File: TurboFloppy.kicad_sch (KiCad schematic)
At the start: 20 parts, among them CN1 SOCKET_28PIN, CN2 PIN_HEADER_28PIN, J1 C16-Exp-Port, Q1 NPN, U1 8255, U2 74LS30, U4 74LS27, U5 74LS10

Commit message: Replace cartridge connector
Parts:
- removed Q1: NPN, Package_TO_SOT_THT:TO-92_HandSolder, symbol Simulation_SPICE:NPN
- added Q1: BC547, Package_TO_SOT_THT:TO-92_HandSolder, symbol Transistor_BJT:BC547
- CN1: renamed from J1; value C16-Exp-Port -> EXPANSION_PORT
- renumbered CN1 to CN2, CN2 to CN3
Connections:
- net GND: now also Q1.3 (E)
- net at R2.2: now also Q1.2 (B)
- net at R1.1, U1.35 (RESET): now also Q1.1 (C)
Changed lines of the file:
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@@
 	(title_block
 		(title "Intel 8255 Interface for the Commodore 16, 116 and Plus/4")
-		(date "2024-07-13")
+		(date "2024-07-14")
 		(rev "1git")
 		(company "SukkoPera")
 		(comment 1 "Based on the article published in Rádiótechnika 1988/12 by Ferenc Garay and Dr. János Rohonczy.")
 		(comment 2 "http://plus4world.powweb.com/publications/Radiotechnika_1988_december")
+		(comment 3 "Licensed under CC BY-NC-SA 4.0")
 	)
 	(junction
@@
 	)
 	(symbol
+		(lib_id "Transistor_BJT:BC547")
+		(at 115.57 36.83 0)
+		(unit 1)
+		(exclude_from_sim no)
+		(in_bom yes)
+		(on_board yes)
+		(dnp no)
+		(fields_autoplaced yes)
+		(property "Reference" "Q1"
+			(at 120.65 35.5599 0)
+			(effects
+				(font
+					(size 1.27 1.27)
+				)
+				(justify left)
+			)
+		)
+		(property "Value" "BC547"
+			(at 120.65 38.0999 0)
+			(effects
+				(font
+					(size 1.27 1.27)
+				)
+				(justify left)
+			)
+		)
+		(property "Footprint" "Package_TO_SOT_THT:TO-92_HandSolder"
+			(at 120.65 38.735 0)
+			(effects
+				(font
+					(size 1.27 1.27)
+					(italic yes)
+				)
+				(justify left)
+				(hide yes)
+			)
+		)
+		(property "Datasheet" "https://www.onsemi.com/pub/Collateral/BC550-D.pdf"
+			(at 115.57 36.83 0)
+			(effects
+				(font
+					(size 1.27 1.27)
+				)
+				(justify left)
+				(hide yes)
+			)
+		)
+		(property "Description" "0.1A Ic, 45V Vce, Small Signal NPN Transistor, TO-92"
+			(at 115.57 36.83 0)
+			(effects
+				(font
+					(size 1.27 1.27)
+				)
+				(hide yes)
+			)
+		)
+		(pin "1"
+		)
+		(pin "2"
+		)
+		(pin "3"
+		)
+		(instances
+			(project ""
+				(path "/0a31112a-e046-4d46-8b9e-0685d05e37f7"
+					(reference "Q1")
+					(unit 1)
+				)
+			)
+		)
+	)
+	(symbol
 		(lib_id "74xx:74LS10")
 		(at 256.54 142.24 0)
@@
 		(on_board yes)
 		(dnp no)
-		(property "Reference" "CN2"
+		(property "Reference" "CN3"
 			(at 259.08 41.91 0)
 			(effects
@@
 			(project ""
 				(path "/0a31112a-e046-4d46-8b9e-0685d05e37f7"
-					(reference "CN2")
+					(reference "CN3")
 					(unit 1)
 				)
@@
 		(dnp no)
 		(fields_autoplaced yes)
-		(property "Reference" "J1"
+		(property "Reference" "CN1"
 			(at 54.61 24.13 0)
 			(effects
@@
 			)
 		)
-		(property "Value" "C16-Exp-Port"
+		(property "Value" "EXPANSION_PORT"
 			(at 54.61 26.67 0)
 			(effects
@@
 			(project ""
 				(path "/0a31112a-e046-4d46-8b9e-0685d05e37f7"
-					(reference "J1")
+					(reference "CN1")
 					(unit 1)
 				)
@@
 	)
 	(symbol
-		(lib_id "Simulation_SPICE:NPN")
-		(at 115.57 36.83 0)
-		(unit 1)
-		(exclude_from_sim no)
-		(in_bom yes)
-		(on_board yes)
-		(dnp no)
-		(property "Reference" "Q1"
-			(at 111.506 39.624 0)
-			(effects
-				(font
-					(size 1.27 1.27)
-				)
-				(justify left)
-			)
-		)
-		(property "Value" "NPN"
-			(at 109.982 41.91 0)
-			(effects
-				(font
-					(size 1.27 1.27)
-				)
-				(justify left)
-			)
-		)
-		(property "Footprint" "Package_TO_SOT_THT:TO-92_HandSolder"
-			(at 179.07 36.83 0)
-			(effects
-				(font
-					(size 1.27 1.27)
-				)
-				(hide yes)
-			)
-		)
-		(property "Datasheet" "https://ngspice.sourceforge.io/docs/ngspice-html-manual/manual.xhtml#cha_BJTs"
-			(at 179.07 36.83 0)
-			(effects
-				(font
-					(size 1.27 1.27)
-				)
-				(hide yes)
-			)
-		)
-		(property "Description" "Bipolar transistor symbol for simulation only, substrate tied to the emitter"
-			(at 115.57 36.83 0)
-			(effects
-				(font
-					(size 1.27 1.27)
-				)
-				(hide yes)
-			)
-		)
-		(property "Sim.Device" "NPN"
-			(at 115.57 36.83 0)
-			(effects
-				(font
-					(size 1.27 1.27)
-				)
-				(hide yes)
-			)
-		)
-		(property "Sim.Type" "GUMMELPOON"
-			(at 115.57 36.83 0)
-			(effects
-				(font
-					(size 1.27 1.27)
-				)
-				(hide yes)
-			)
-		)
-		(property "Sim.Pins" "1=C 2=B 3=E"
-			(at 115.57 36.83 0)
-			(effects
-				(font
-					(size 1.27 1.27)
-				)
-				(hide yes)
-			)
-		)
-		(pin "3"
-		)
-		(pin "2"
-		)
-		(pin "1"
-		)
-		(instances
-			(project ""
-				(path "/0a31112a-e046-4d46-8b9e-0685d05e37f7"
-					(reference "Q1")
-					(unit 1)
-				)
-			)
-		)
-	)
-	(symbol
 		(lib_id "power:+5V")
 		(at 267.97 39.37 0)
@@
 		(dnp no)
 		(fields_autoplaced yes)
-		(property "Reference" "CN1"
+		(property "Reference" "CN2"
 			(at 217.17 60.9599 0)
 			(effects
@@
 			(project ""
 				(path "/0a31112a-e046-4d46-8b9e-0685d05e37f7"
-					(reference "CN1")
+					(reference "CN2")
 					(unit 1)
 				)

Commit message: Who knows?
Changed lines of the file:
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@@
 		(rev "1git")
 		(company "SukkoPera")
-		(comment 1 "Based on the article published in Rádiótechnika 1988/12 by Ferenc Garay and Dr. János Rohonczy.")
+		(comment 1 "Based on the article published in Rádiótechnika 1988/12 by Ferenc Garay and Dr. János Rohonczy")
 		(comment 2 "http://plus4world.powweb.com/publications/Radiotechnika_1988_december")
 		(comment 3 "Licensed under CC BY-NC-SA 4.0")
@@
 		(on_board yes)
 		(dnp no)
-		(fields_autoplaced yes)
 		(property "Reference" "Q1"
-			(at 120.65 35.5599 0)
+			(at 111.506 39.624 0)
 			(effects
 				(font
@@
 		)
 		(property "Value" "BC547"
-			(at 120.65 38.0999 0)
+			(at 107.696 41.91 0)
 			(effects
 				(font

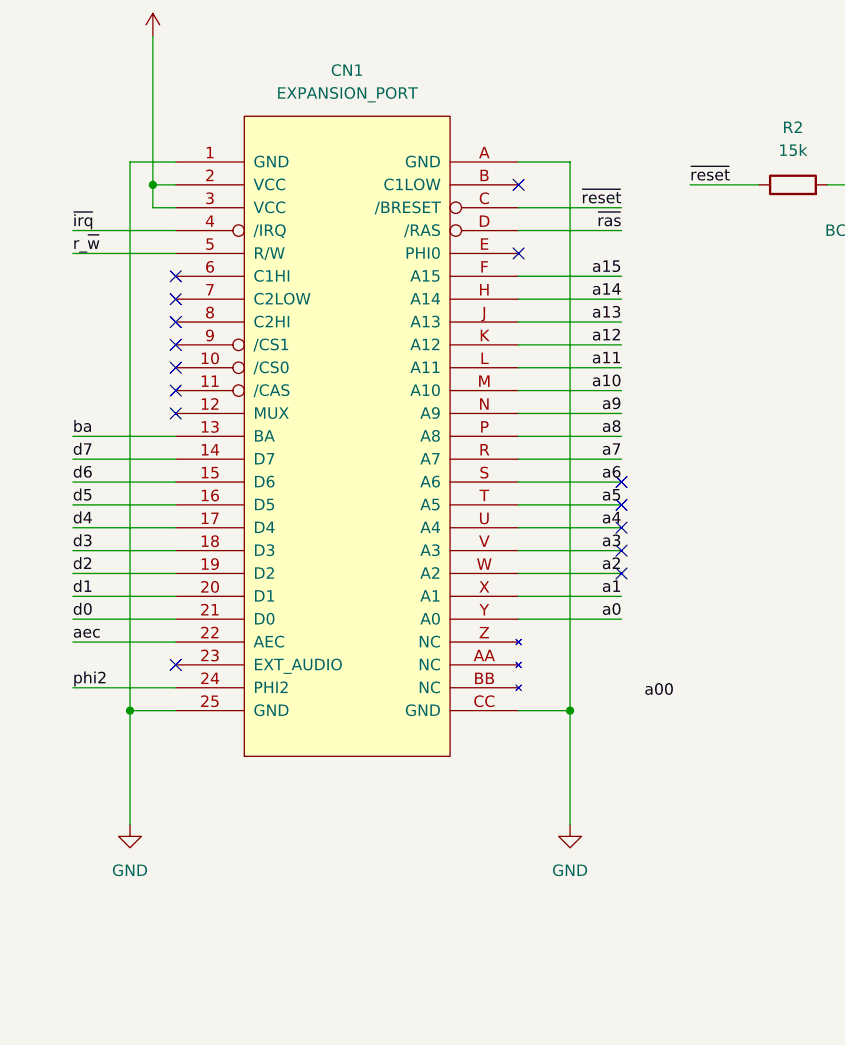
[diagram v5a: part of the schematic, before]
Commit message: Fix connector symbol and ERC
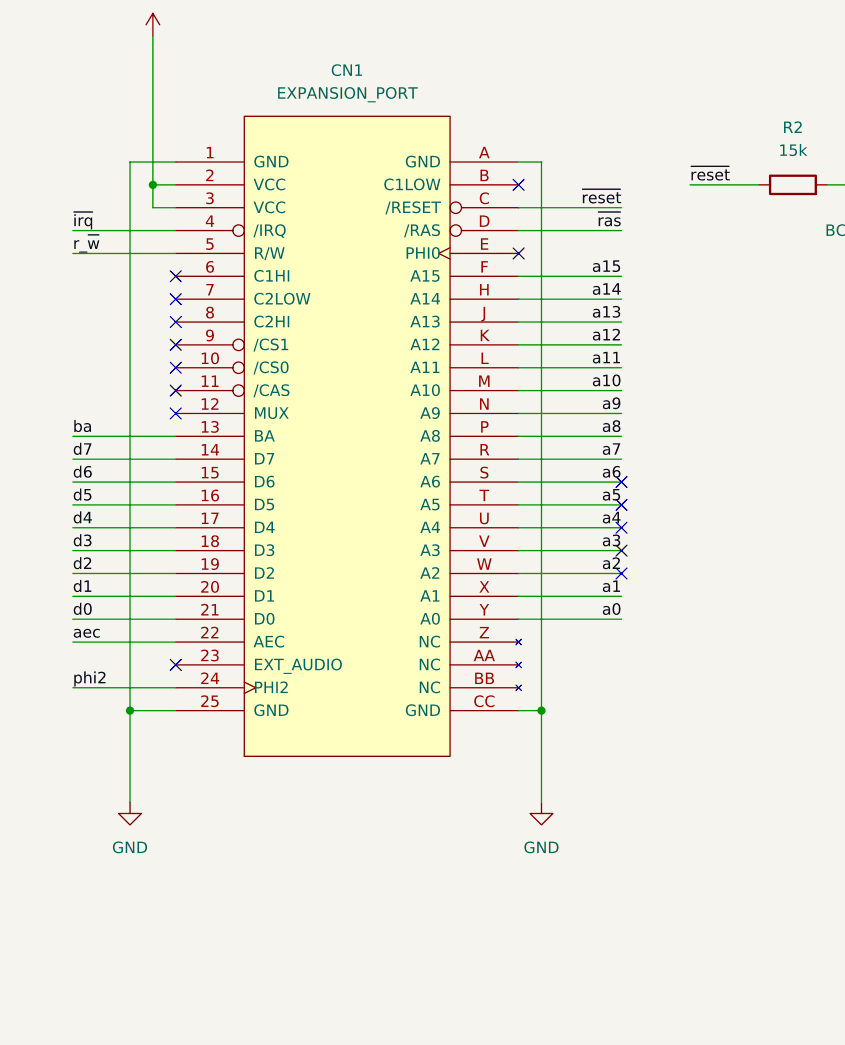
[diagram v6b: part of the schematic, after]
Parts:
- CN1: footprint TurboFloppy:C16_Cart_Conn -> MODULE
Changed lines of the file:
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@@
 	)
 	(junction
-		(at 79.375 95.25)
-		(diameter 0)
-		(color 0 0 0 0)
-	)
-	(junction
 		(at 35.56 160.02)
 		(diameter 0)
@@
 	)
 	(junction
+		(at 76.2 95.25)
+		(diameter 0)
+		(color 0 0 0 0)
+	)
+	(junction
 		(at 250.19 81.28)
 		(diameter 0)
@@
 	(wire
 		(pts
+			(xy 76.2 34.29) (xy 76.2 95.25)
+		)
+		(stroke
+			(width 0)
+			(type default)
+		)
+	)
+	(wire
+		(pts
 			(xy 24.13 72.39) (xy 35.56 72.39)
 		)
@@
 	(wire
 		(pts
+			(xy 73.66 95.25) (xy 76.2 95.25)
+		)
+		(stroke
+			(width 0)
+			(type default)
+		)
+	)
+	(wire
+		(pts
 			(xy 229.87 144.78) (xy 248.92 144.78)
 		)
@@
 	(wire
 		(pts
-			(xy 79.375 95.25) (xy 73.66 95.25)
-		)
-		(stroke
-			(width 0)
-			(type default)
-		)
-	)
-	(wire
-		(pts
 			(xy 170.18 35.56) (xy 180.34 35.56)
 		)
@@
 	(wire
 		(pts
-			(xy 79.375 34.29) (xy 79.375 95.25)
-		)
-		(stroke
-			(width 0)
-			(type default)
-		)
-	)
-	(wire
-		(pts
 			(xy 85.09 80.01) (xy 73.66 80.01)
 		)
@@
 	(wire
 		(pts
+			(xy 76.2 95.25) (xy 76.2 105.41)
+		)
+		(stroke
+			(width 0)
+			(type default)
+		)
+	)
+	(wire
+		(pts
 			(xy 201.93 81.28) (xy 210.82 81.28)
 		)
@@
 	(wire
 		(pts
-			(xy 30.48 95.25) (xy 30.48 107.95)
+			(xy 30.48 95.25) (xy 30.48 105.41)
 		)
 		(stroke
@@
 	(wire
 		(pts
-			(xy 73.66 34.29) (xy 79.375 34.29)
+			(xy 73.66 34.29) (xy 76.2 34.29)
 		)
 		(stroke
@@
 	(wire
 		(pts
-			(xy 79.375 95.25) (xy 79.375 107.95)
-		)
-		(stroke
-			(width 0)
-			(type default)
-		)
-	)
-	(wire
-		(pts
 			(xy 106.68 186.69) (xy 106.68 187.96)
 		)
@@
 		)
 	)
-	(label "a00"
-		(at 87.63 93.98 0)
-		(fields_autoplaced yes)
-		(effects
-			(font
-				(size 1.27 1.27)
-			)
-			(justify left bottom)
-		)
-	)
 	(label "pb2"
 		(at 274.32 76.2 180)
@@
 	(symbol
 		(lib_id "power:GND")
-		(at 30.48 107.95 0)
+		(at 30.48 105.41 0)
+		(mirror y)
 		(unit 1)
 		(exclude_from_sim no)
@@
 		(on_board yes)
 		(dnp no)
-		(fields_autoplaced yes)
 		(property "Reference" "#PWR04"
-			(at 30.48 114.3 0)
+			(at 30.48 111.76 0)
 			(effects
 				(font
@@
 		)
 		(property "Value" "GND"
-			(at 30.48 113.03 0)
+			(at 30.48 110.49 0)
 			(effects
 				(font
@@
 		)
 		(property "Footprint" ""
-			(at 30.48 107.95 0)
+			(at 30.48 105.41 0)
 			(effects
 				(font
@@
 		)
 		(property "Datasheet" ""
-			(at 30.48 107.95 0)
+			(at 30.48 105.41 0)
 			(effects
 				(font
@@
 		)
 		(property "Description" "Power symbol creates a global label with name \"GND\" , ground"
-			(at 30.48 107.95 0)
+			(at 30.48 105.41 0)
 			(effects
 				(font
@@
 			)
 		)
-		(property "Footprint" "TurboFloppy:C16_Cart_Conn"
+		(property "Footprint" "MODULE"
 			(at 54.61 106.68 0)
 			(effects
@@
 	(symbol
 		(lib_id "power:GND")
-		(at 79.375 107.95 0)
+		(at 76.2 105.41 0)
 		(mirror y)
 		(unit 1)
@@
 		(fields_autoplaced yes)
 		(property "Reference" "#PWR05"
-			(at 79.375 114.3 0)
+			(at 76.2 111.76 0)
 			(effects
 				(font
@@
 		)
 		(property "Value" "GND"
-			(at 79.375 113.03 0)
+			(at 76.2 110.49 0)
 			(effects
 				(font
@@
 		)
 		(property "Footprint" ""
-			(at 79.375 107.95 0)
+			(at 76.2 105.41 0)
 			(effects
 				(font
@@
 		)
 		(property "Datasheet" ""
-			(at 79.375 107.95 0)
+			(at 76.2 105.41 0)
 			(effects
 				(font
@@
 		)
 		(property "Description" "Power symbol creates a global label with name \"GND\" , ground"
-			(at 79.375 107.95 0)
+			(at 76.2 105.41 0)
 			(effects
 				(font
